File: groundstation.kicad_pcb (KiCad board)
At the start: 2 copper layers, 10 parts, among them J1 USB_C_Receptacle_USB2.0_16P, J2 62684-402100ALF, SW1 SW_Push, U1 ESP32-S3-WROOM-1

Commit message: Update schematicand PCB
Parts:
- removed J2: 62684-402100ALF, 62684:CONN_62684-402100ALF_AMP
- added 2.2uF: C10, Capacitor_SMD:C_0402_1005Metric, F.Cu at (128.9, 61.0)
- added C11: 2.2uF, Capacitor_SMD:C_0402_1005Metric, F.Cu at (125.9, 61.0)
- added C2: 1uF, Capacitor_SMD:C_0402_1005Metric, F.Cu at (137.4, 61.0)
- added C3: 1uF, Capacitor_SMD:C_0402_1005Metric, F.Cu at (135.9, 61.0)
- added C4: 1uF, Capacitor_SMD:C_0402_1005Metric, F.Cu at (134.4, 61.0)
- added C5: 1uF, Capacitor_SMD:C_0402_1005Metric, F.Cu at (132.9, 61.0)
- added C6: 1uF, Capacitor_SMD:C_0402_1005Metric, F.Cu at (131.4, 61.0)
- added C9: 2.2uF, Capacitor_SMD:C_0402_1005Metric, F.Cu at (123.4, 61.0)
- added DS1: NHD-C12832A1Z-FSW-FBW-3V3, Ground_Station:LCD_NHD-C12832A1Z-FSW-FBW-3V3, F.Cu at (125.4, 76.5)
- C1: value C_Small_US -> 0.1uF; footprint Capacitor_THT:C_Disc_D3.0mm_W1.6mm_P2.50mm -> Capacitor_SMD:C_0402_1005Metric
- R5: value R_Small -> 3.3k
- U1: moved to F.Cu
- moved R4 55.2 mm to (108.5, 43.0)
- moved R3 54.7 mm to (108.5, 41.5)
- moved R2 54.3 mm to (108.5, 40.0)
- moved R1 53.8 mm to (108.5, 38.5)
- moved J1 32.8 mm to (109.9, 52.4), turned to -90 degrees
- moved C1 26.8 mm to (108.5, 45.0)
- moved R5 22.2 mm to (113.5, 61.0)
- moved SW1 19.3 mm to (108.5, 61.0)
- moved U1 16.1 mm to (127.5, 43.5), turned to 0 degrees
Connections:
- net GND renamed Vss
- U1 pad 15: unconnected-(U1-IO3-Pad15) -> SCL
- U1 pad 2: +3V3 -> VDD
- U1 pad 27: unconnected-(U1-IO0-Pad27) -> CS1
- U1 pad 38: unconnected-(U1-IO2-Pad38) -> A0
- U1 pad 39: unconnected-(U1-IO1-Pad39) -> RST
- U1 pad 4: unconnected-(U1-IO4-Pad4) -> SI

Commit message: done with schematic (hopefully)
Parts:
- removed 2.2uF: C10, Capacitor_SMD:C_0402_1005Metric
- removed C1: 0.1uF, Capacitor_SMD:C_0402_1005Metric
- added 2.2uF1: C_Small_US, Capacitor_SMD:C_0402_1005Metric, F.Cu at (170.6, 32.7)
- added 2.2uF2: C_Small_US, Capacitor_SMD:C_0402_1005Metric, F.Cu at (170.6, 34.7)
- added C12: 10u, Capacitor_SMD:C_0805_2012Metric, F.Cu at (171.1, 81.0)
- added LED1: LTST-C170KRKT, Ground_Station:LED_LTST-C170KRKT_LTO-M, F.Cu at (166.2, 78.2)
- added R6: 410, Resistor_SMD:R_0402_1005Metric, F.Cu at (170.6, 26.8)
- added R7: 10k, Resistor_SMD:R_0402_1005Metric, F.Cu at (170.6, 28.8)
- added U3: AMS1117-3.3, Package_TO_SOT_SMD:SOT-223-3_TabPin2, F.Cu at (168.0, 72.4)
- C11: value 2.2uF -> 22u; footprint Capacitor_SMD:C_0402_1005Metric -> Capacitor_SMD:C_0805_2012Metric
- C2, C3, C4, C5, C6: value 1uF -> 1u
- R1, R2, R3, R4: moved to F.Cu
- R5: value 3.3k -> 0; footprint Capacitor_THT:C_Disc_D3.0mm_W1.6mm_P2.50mm -> Resistor_SMD:R_0402_1005Metric
- moved SW1 69.1 mm to (170.6, 30.8)
- moved R5 67.6 mm to (170.6, 24.8)
- moved R1 65.8 mm to (170.6, 16.8), turned to 0 degrees
- moved R2 65.7 mm to (170.6, 18.8), turned to 0 degrees
- moved R3 65.5 mm to (170.6, 20.8), turned to 0 degrees
- moved R4 65.3 mm to (170.6, 22.8), turned to 0 degrees
- moved J1 60.1 mm to (168.9, 63.5), turned to 0 degrees
- moved C9 49.4 mm to (170.6, 46.5)
- moved C11 48.2 mm to (171.1, 78.0), turned to 0 degrees
- moved C6 42.5 mm to (170.6, 44.6), turned to 0 degrees
- moved C5 42.0 mm to (170.6, 42.6), turned to 0 degrees
- moved C4 41.6 mm to (170.6, 40.6), turned to 0 degrees
- moved C3 41.3 mm to (170.6, 38.6), turned to 0 degrees
- moved C2 41.2 mm to (170.6, 36.7), turned to 0 degrees
- moved U1 17.2 mm to (144.7, 44.1)
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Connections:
- net Net-(U1-EN) renamed EN
- C11 pad 1: Net-(DS1-C1+) -> VDD
- C11 pad 2: Net-(DS1-C1-) -> Vss
- C2 pad 1: Vss -> V0
- C2 pad 2: V0 -> Vss
- C3 pad 1: Vss -> V1
- C3 pad 2: V1 -> Vss
- C4 pad 1: Vss -> V2
- C4 pad 2: V2 -> Vss
- C5 pad 1: Vss -> V3
- C5 pad 2: V3 -> Vss
- C6 pad 1: Vss -> V4
- C6 pad 2: V4 -> Vss
- DS1 pad A: Vss -> VDD

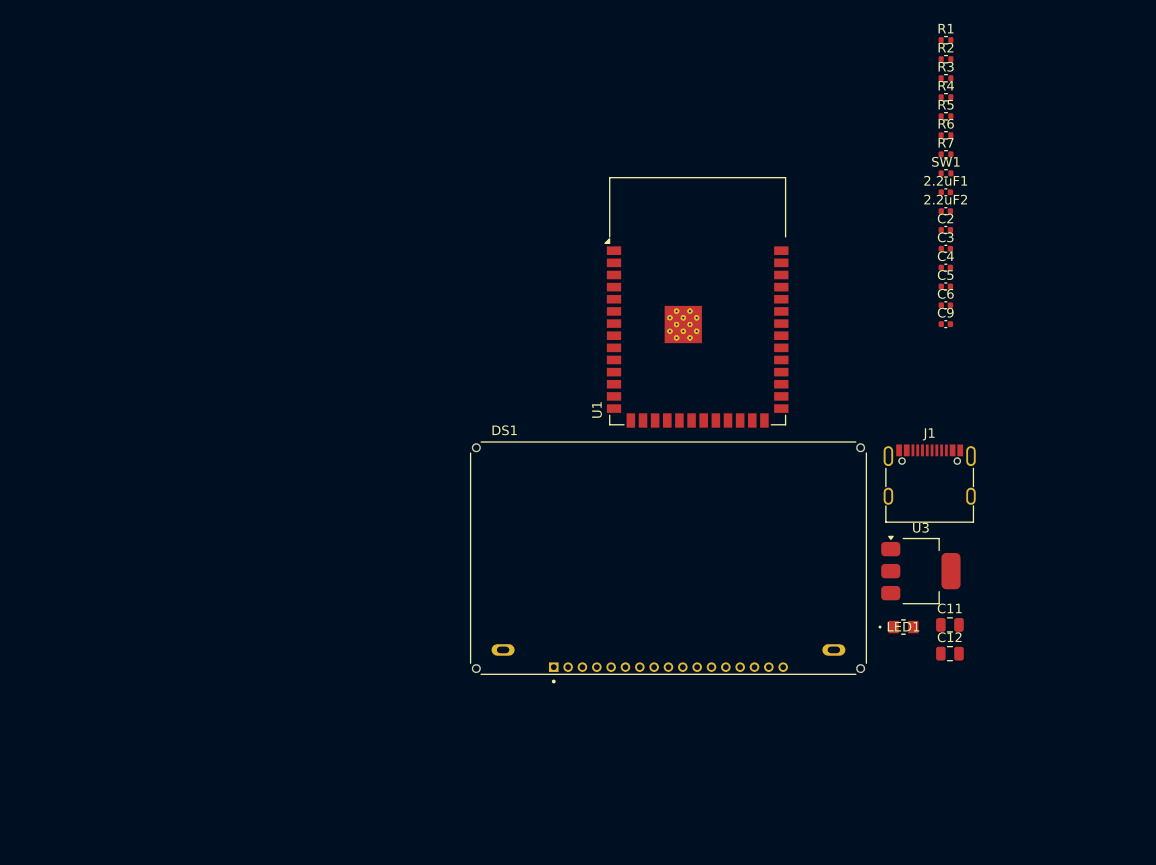
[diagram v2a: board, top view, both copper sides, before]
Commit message: added GPS module
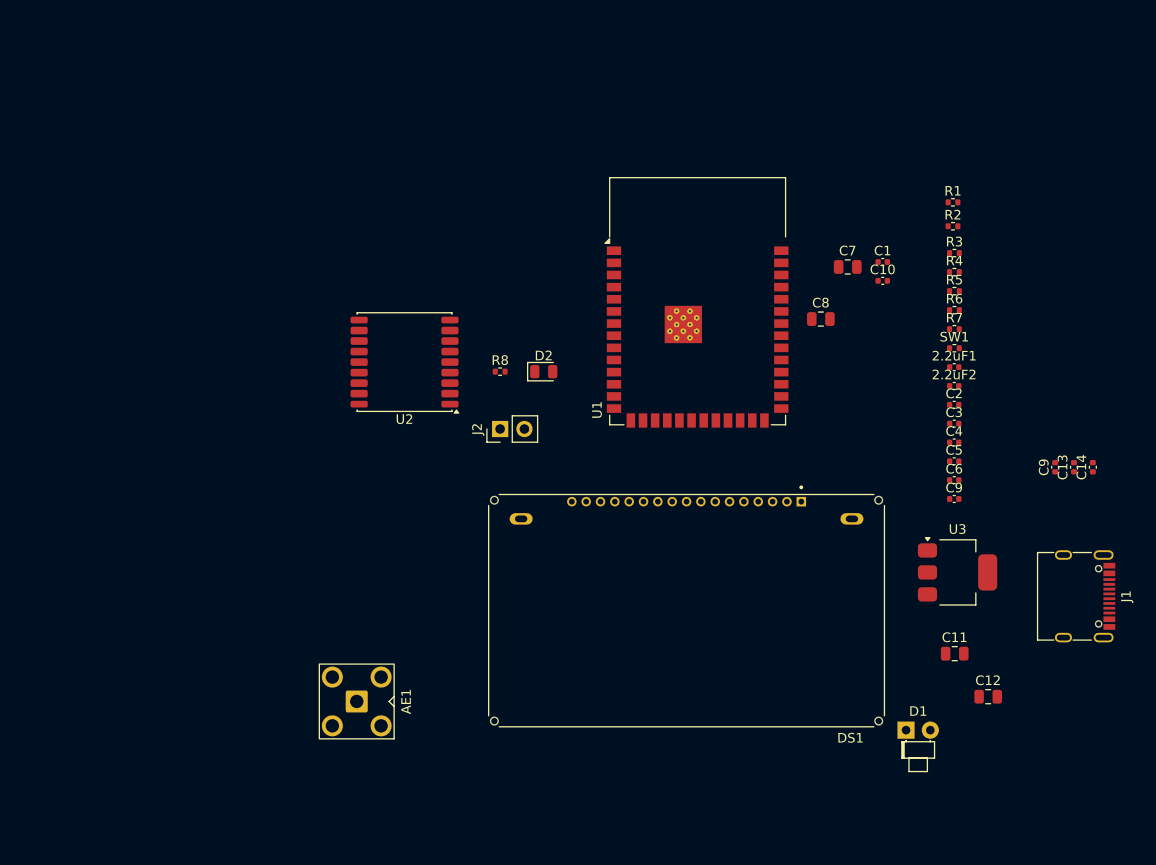
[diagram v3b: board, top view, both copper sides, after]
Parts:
- removed LED1: LTST-C170KRKT, Ground_Station:LED_LTST-C170KRKT_LTO-M
- added AE1: Antenna, Connector_Coaxial:SMA_BAT_Wireless_BWSMA-KWE-Z001, F.Cu at (109.0, 86.0)
- added C1: 0.1u, Capacitor_SMD:C_0402_1005Metric, F.Cu at (164.0, 40.0)
- added C10: 1u, Capacitor_SMD:C_0402_1005Metric, F.Cu at (164.0, 42.0)
- added C13: 2.2uF, Capacitor_SMD:C_0402_1005Metric, F.Cu at (184.0, 61.5)
- added C14: 2.2uF, Capacitor_SMD:C_0402_1005Metric, F.Cu at (186.0, 61.5)
- added C7: 10uF, Capacitor_SMD:C_0805_2012Metric, F.Cu at (160.4, 40.5)
- added C8: 0.1u, Capacitor_SMD:C_0805_2012Metric, F.Cu at (157.6, 46.0)
- added C9: 1u, Capacitor_SMD:C_0402_1005Metric, F.Cu at (182.1, 61.5)
- added D1: LED, LED_THT:LED_D1.8mm_W1.8mm_H2.4mm_Horizontal_O1.27mm_Z1.6mm, F.Cu at (166.5, 89.0)
- added D2: LED, LED_SMD:LED_0805_2012Metric, F.Cu at (128.6, 51.5)
- added J2: Conn_01x02_Pin, Connector_PinHeader_2.54mm:PinHeader_1x02_P2.54mm_Vertical, F.Cu at (124.0, 57.5)
- added R8: 1k, Resistor_SMD:R_0402_1005Metric, F.Cu at (124.0, 51.5)
- added U2: MAX-M10S, RF_GPS:ublox_MAX, F.Cu at (114.0, 50.5)
- C2: value 1u -> 2.2u
- C5: value 1u -> 1.0u
- moved J1 19.0 mm to (184.0, 75.0), turned to -90 degrees
- moved R3 18.3 mm to (171.5, 39.1)
- moved R4 18.3 mm to (171.5, 41.1)
- moved R7 18.3 mm to (171.5, 47.1)
- moved 2.2uF1 18.3 mm to (171.5, 51.0)
- moved 2.2uF2 18.3 mm to (171.5, 53.0)
- moved C2 18.3 mm to (171.5, 55.0)
- moved C3 18.3 mm to (171.5, 56.9)
- moved C4 18.3 mm to (171.5, 58.9)
- moved C5 18.3 mm to (171.5, 60.9)
- moved C6 18.3 mm to (171.5, 62.9)
- moved R5 18.3 mm to (171.5, 43.1)
- moved R6 18.3 mm to (171.5, 45.1)
- moved SW1 18.3 mm to (171.5, 49.0)
- moved C9 18.3 mm to (171.5, 64.8)
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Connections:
- net SI renamed Display_SI
- net VBUS renamed 5V
- net VDD renamed +3V3
- C11 pad 2: Vss -> GND
- C12 pad 2: Vss -> GND
- C2 pad 1: V0 -> Net-(DS1-VOUT)
- C2 pad 2: Vss -> GND
- C3 pad 1: V1 -> Net-(DS1-V4)
- C3 pad 2: Vss -> GND
- C4 pad 1: V2 -> Net-(DS1-V3)
- C4 pad 2: Vss -> GND
- C5 pad 1: V3 -> Net-(DS1-V2)
- C5 pad 2: Vss -> GND
- C6 pad 1: V4 -> Net-(DS1-V1)
- C6 pad 2: Vss -> GND
- DS1 pad 1: V0 -> Net-(DS1-V0)
- DS1 pad 10: Vout -> Net-(DS1-VOUT)
- DS1 pad 11: Vss -> GND
- DS1 pad 15: A0 -> Display_A0
- DS1 pad 16: RST -> Display_RST
- DS1 pad 17: CS1 -> Display_CS1
- DS1 pad 2: V1 -> Net-(DS1-V1)
- DS1 pad 3: V2 -> Net-(DS1-V2)
- DS1 pad 4: V3 -> Net-(DS1-V3)
- DS1 pad 5: V4 -> Net-(DS1-V4)
- DS1 pad K: Vss -> GND
- J1 pad A1: Vss -> GND
- J1 pad A12: Vss -> GND
- J1 pad B1: Vss -> GND
- J1 pad B12: Vss -> GND
- J1 pad S1: Vss -> GND
- R3 pad 1: Vss -> GND
- R4 pad 1: Vss -> GND
- R6 pad 1: Vss -> GND
- SW1 pad 1: Vss -> GND
- U1 pad 1: Vss -> GND
- U1 pad 15: SCL -> Display_A0
- U1 pad 21: unconnected-(U1-IO13-Pad21) -> SDA
- U1 pad 22: unconnected-(U1-IO14-Pad22) -> SCL
- U1 pad 27: CS1 -> Net-(J2-Pin_1)
- U1 pad 38: A0 -> Display_RST
- U1 pad 39: RST -> Display_CS1
- U1 pad 40: Vss -> GND
- U1 pad 41: Vss -> GND
- U1 pad 5: unconnected-(U1-IO5-Pad5) -> /EXTINT
- U3 pad 1: Vss -> GND

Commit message: dunno, random adds
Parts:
- moved AE1 39.1 mm to (96.5, 49.0), turned to 90 degrees
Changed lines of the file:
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@@
 	(footprint "Connector_Coaxial:SMA_BAT_Wireless_BWSMA-KWE-Z001"
 		(layer "F.Cu")
-		(at 109 86 180)
+		(at 96.45 48.95 90)
 		(descr "BAT Wireless BWSMA-KWE-Z00 https://www.lcsc.com/datasheet/lcsc_datasheet_2310171703_BAT-WIRELESS-BWSMA-KWE-Z001_C496551.pdf")
 		(tags "SMA THT Female Jack Horizontal")
 		(property "Reference" "AE1"
-			(at -5.2 0 90)
+			(at -5.2 0 0)
 			(layer "F.SilkS")
 			(effects
@@
 		)
 		(property "Value" "Antenna"
-			(at 0 5 0)
+			(at 0 5 90)
 			(layer "F.Fab")
 			(effects
@@
 		)
 		(property "Datasheet" "~"
-			(at 0 0 180)
+			(at 0 0 90)
 			(unlocked yes)
 			(layer "F.Fab")
@@
 		)
 		(property "Description" "Antenna"
-			(at 0 0 180)
+			(at 0 0 90)
 			(unlocked yes)
 			(layer "F.Fab")
@@
 		)
 		(fp_line
+			(start 2.5 -11.5)
+			(end 2.5 -3)
+			(stroke
+				(width 0.1)
+				(type solid)
+			)
+			(layer "F.Fab")
+		)
+		(fp_line
+			(start -2.5 -11.5)
+			(end 2.5 -11.5)
+			(stroke
+				(width 0.1)
+				(type solid)
+			)
+			(layer "F.Fab")
+		)
+		(fp_line
+			(start -2.5 -11.5)
+			(end -2.5 -3)
+			(stroke
+				(width 0.1)
+				(type solid)
+			)
+			(layer "F.Fab")
+		)
+		(fp_line
+			(start -3 -9.5)
+			(end 3 -10)
+			(stroke
+				(width 0.1)
+				(type solid)
+			)
+			(layer "F.Fab")
+		)
+		(fp_line
+			(start -3 -9)
+			(end 3 -9.5)
+			(stroke
+				(width 0.1)
+				(type solid)
+			)
+			(layer "F.Fab")
+		)
+		(fp_line
+			(start -3 -8.5)
+			(end 3 -9)
+			(stroke
+				(width 0.1)
+				(type solid)
+			)
+			(layer "F.Fab")
+		)
+		(fp_line
+			(start -3 -8)
+			(end 3 -8.5)
+			(stroke
+				(width 0.1)
+				(type solid)
+			)
+			(layer "F.Fab")
+		)
+		(fp_line
+			(start -3 -7.5)
+			(end 3 -8)
+			(stroke
+				(width 0.1)
+				(type solid)
+			)
+			(layer "F.Fab")
+		)
+		(fp_line
+			(start -3 -7)
+			(end 3 -7.5)
+			(stroke
+				(width 0.1)
+				(type solid)
+			)
+			(layer "F.Fab")
+		)
+		(fp_line
 			(start 3 -3)
 			(end 3 3)
@@
 		)
 		(fp_line
-			(start 2.5 -11.5)
-			(end 2.5 -3)
+			(start -3 -3)
+			(end 3 -3)
+			(stroke
+				(width 0.1)
+				(type solid)
+			)
+			(layer "F.Fab")
+		)
+		(fp_line
+			(start -3 -3)
+			(end -3 3)
+			(stroke
+				(width 0.1)
+				(type solid)
+			)
+			(layer "F.Fab")
+		)
+		(fp_line
+			(start -3 -1)
+			(end -2 0)
 			(stroke
 				(width 0.1)
@@
 		)
 		(fp_line
-			(start -2.5 -11.5)
-			(end 2.5 -11.5)
-			(stroke
-				(width 0.1)
-				(type solid)
-			)
-			(layer "F.Fab")
-		)
-		(fp_line
-			(start -2.5 -11.5)
-			(end -2.5 -3)
-			(stroke
-				(width 0.1)
-				(type solid)
-			)
-			(layer "F.Fab")
-		)
-		(fp_line
 			(start -3 3)
 			(end 3 3)
@@
 			(layer "F.Fab")
 		)
-		(fp_line
-			(start -3 -1)
-			(end -2 0)
-			(stroke
-				(width 0.1)
-				(type solid)
-			)
-			(layer "F.Fab")
-		)
-		(fp_line
-			(start -3 -3)
-			(end 3 -3)
-			(stroke
-				(width 0.1)
-				(type solid)
-			)
-			(layer "F.Fab")
-		)
-		(fp_line
-			(start -3 -3)
-			(end -3 3)
-			(stroke
-				(width 0.1)
-				(type solid)
-			)
-			(layer "F.Fab")
-		)
-		(fp_line
-			(start -3 -7)
-			(end 3 -7.5)
-			(stroke
-				(width 0.1)
-				(type solid)
-			)
-			(layer "F.Fab")
-		)
-		(fp_line
-			(start -3 -7.5)
-			(end 3 -8)
-			(stroke
-				(width 0.1)
-				(type solid)
-			)
-			(layer "F.Fab")
-		)
-		(fp_line
-			(start -3 -8)
-			(end 3 -8.5)
-			(stroke
-				(width 0.1)
-				(type solid)
-			)
-			(layer "F.Fab")
-		)
-		(fp_line
-			(start -3 -8.5)
-			(end 3 -9)
-			(stroke
-				(width 0.1)
-				(type solid)
-			)
-			(layer "F.Fab")
-		)
-		(fp_line
-			(start -3 -9)
-			(end 3 -9.5)
-			(stroke
-				(width 0.1)
-				(type solid)
-			)
-			(layer "F.Fab")
-		)
-		(fp_line
-			(start -3 -9.5)
-			(end 3 -10)
-			(stroke
-				(width 0.1)
-				(type solid)
-			)
-			(layer "F.Fab")
-		)
 		(fp_text user "${REFERENCE}"
-			(at 0 0 0)
+			(at 0 0 90)
 			(layer "F.Fab")
 			(effects
@@
 		)
 		(pad "1" thru_hole roundrect
-			(at 0 0 180)
+			(at 0 0 90)
 			(size 2.3 2.3)
 			(drill 1.4)
@@
 		)
 		(pad "2" thru_hole circle
-			(at -2.55 -2.55 180)
-			(size 2.2 2.2)
-			(drill 1.4)
-			(layers "*.Cu" "*.Mask")
-			(remove_unused_layers yes)
-			(keep_end_layers yes)
-			(zone_layer_connections)
-		)
-		(pad "2" thru_hole circle
-			(at -2.55 2.55 180)
-			(size 2.2 2.2)
-			(drill 1.4)
-			(layers "*.Cu" "*.Mask")
-			(remove_unused_layers yes)
-			(keep_end_layers yes)
-			(zone_layer_connections)
-		)
-		(pad "2" thru_hole circle
-			(at 2.55 -2.55 180)
-			(size 2.2 2.2)
-			(drill 1.4)
-			(layers "*.Cu" "*.Mask")
-			(remove_unused_layers yes)
-			(keep_end_layers yes)
-			(zone_layer_connections)
-		)
-		(pad "2" thru_hole circle
-			(at 2.55 2.55 180)
-			(size 2.2 2.2)
-			(drill 1.4)
+			(at -2.55 -2.55 90)
+			(size 2.2 2.2)
+			(drill 1.4)
+			(layers "*.Cu" "*.Mask")
+			(remove_unused_layers yes)
+			(keep_end_layers yes)
+			(zone_layer_connections)
+		)
+		(pad "2" thru_hole circle
+			(at -2.55 2.55 90)
+			(size 2.2 2.2)
+			(drill 1.4)
+			(layers "*.Cu" "*.Mask")
+			(remove_unused_layers yes)
+			(keep_end_layers yes)
+			(zone_layer_connections)
+		)
+		(pad "2" thru_hole circle
+			(at 2.55 -2.55 90)
+			(size 2.2 2.2)
+			(drill 1.4)
+			(layers "*.Cu" "*.Mask")
+			(remove_unused_layers yes)
+			(keep_end_layers yes)
+			(zone_layer_connections)
+		)
+		(pad "2" thru_hole circle
+			(at 2.55 2.55 90)
+			(size 2.2 2.2)
+			(drill 1.4)
